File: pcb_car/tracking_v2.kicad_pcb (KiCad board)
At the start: 2 copper layers, 95 x 70 mm, 20 parts, among them J1 Conn_01x02, J2 Conn_01x20_Female, J3 Conn_01x20_Female, J4 Conn_01x02, J5 Conn_01x02, J6 Conn_01x02, J7 Conn_01x02, J8 Conn_01x03, J9 Conn_01x03, SW1 SW_Push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

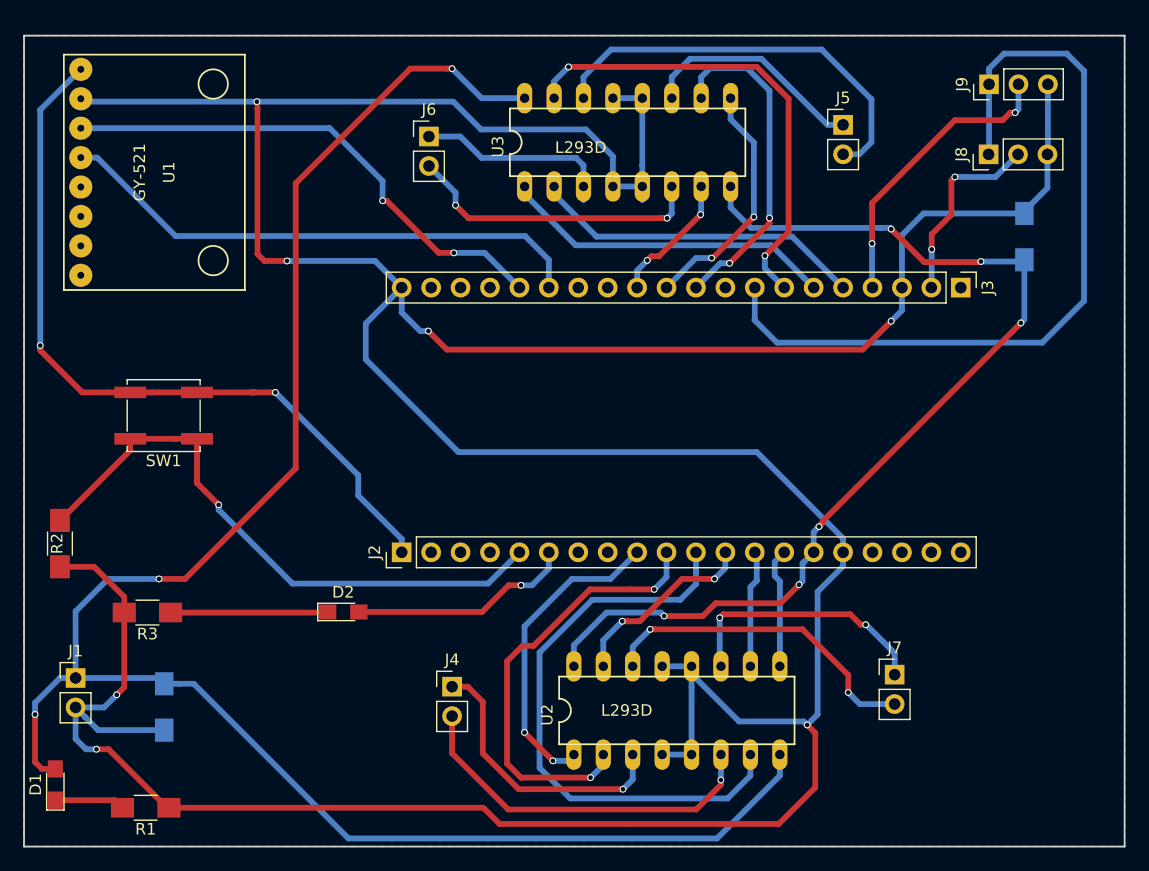
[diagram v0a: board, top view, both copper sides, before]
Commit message: Added second iteration of PCB design (incomplete), moved libraries to subfolder
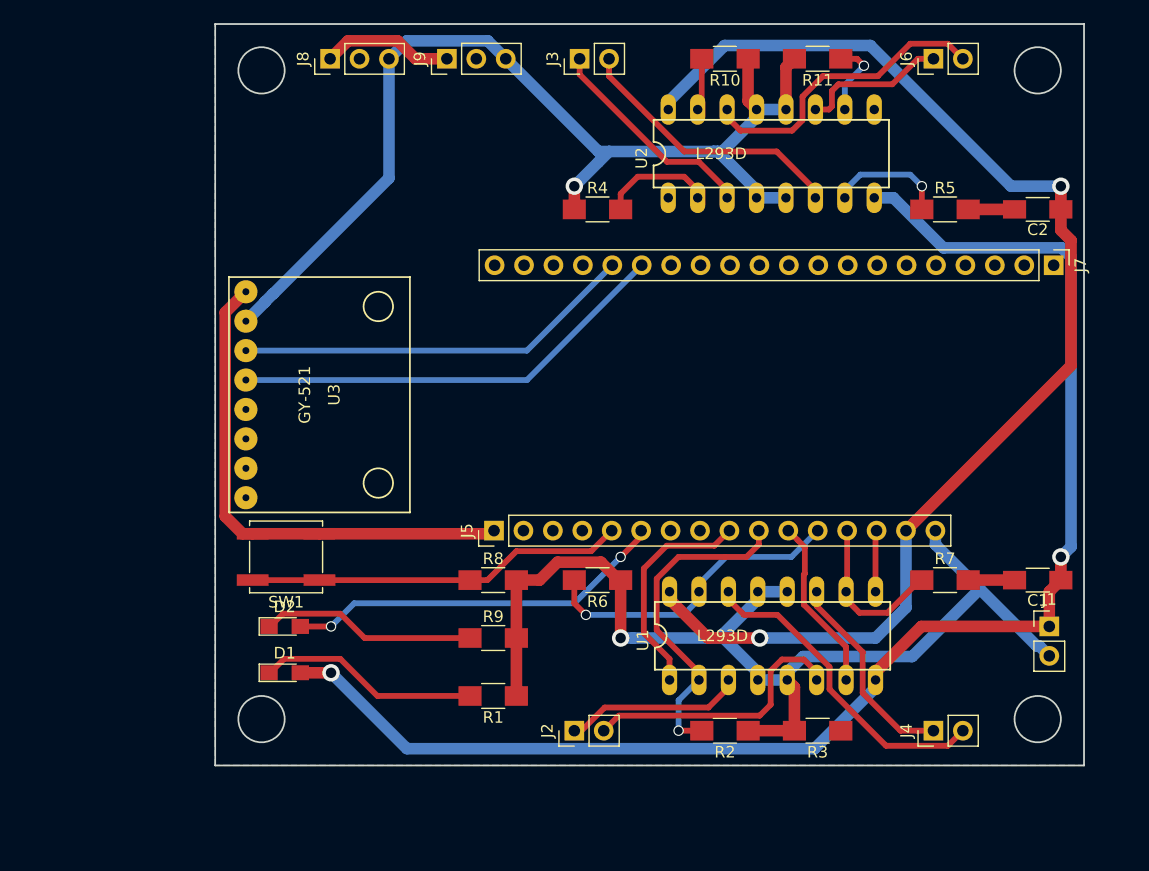
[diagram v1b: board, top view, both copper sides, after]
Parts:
- added R10: R, Resistors_SMD:R_1206_HandSoldering, F.Cu at (163.0, 77.0)
- added R11: R, Resistors_SMD:R_1206_HandSoldering, F.Cu at (171.0, 77.0)
- added R4: R, Resistors_SMD:R_1206_HandSoldering, F.Cu at (152.0, 90.0)
- added R5: R, Resistors_SMD:R_1206_HandSoldering, F.Cu at (182.0, 90.0)
- added R6: R, Resistors_SMD:R_1206_HandSoldering, F.Cu at (152.0, 122.0)
- added R7: R, Resistors_SMD:R_1206_HandSoldering, F.Cu at (182.0, 122.0)
- added R8: R, Resistors_SMD:R_1206_HandSoldering, F.Cu at (143.0, 122.0)
- added R9: R, Resistors_SMD:R_1206_HandSoldering, F.Cu at (143.0, 127.0)
- C1, C2: moved to F.Cu
- J2, J3: value Conn_01x20_Female -> Conn_01x02; footprint Socket_Strips:Socket_Strip_Straight_1x20_Pitch2.54mm -> Pin_Headers:Pin_Header_Straight_1x02_Pitch2.54mm
- J5: value Conn_01x02 -> Conn_01x16_Female; footprint Pin_Headers:Pin_Header_Straight_1x02_Pitch2.54mm -> Socket_Strips:Socket_Strip_Straight_1x16_Pitch2.54mm
- J7: value Conn_01x02 -> Conn_01x20_Female; footprint Pin_Headers:Pin_Header_Straight_1x02_Pitch2.54mm -> Socket_Strips:Socket_Strip_Straight_1x20_Pitch2.54mm
- U1: value GY-521 -> L293D; footprint GY-521:GY-521 -> L293D:DIL16
- U3: value L293D -> GY-521; footprint L293D:DIL16 -> GY-521:GY-521
- moved J1 84.2 mm to (191.0, 126.0)
- moved C1 76.2 mm to (190.0, 122.0), turned to 180 degrees
- moved U1 66.7 mm to (167.1, 126.8), turned to 0 degrees
- moved R2 59.6 mm to (163.0, 135.0), turned to 180 degrees
- moved R3 58.7 mm to (171.0, 135.0)
- moved J8 57.4 mm to (128.9, 77.0)
- moved U2 48.7 mm to (167.0, 85.2)
- moved J9 46.9 mm to (139.0, 77.0)
- moved J5 46.2 mm to (143.1, 117.7), turned to 90 degrees
- moved J6 44.1 mm to (181.0, 77.0), turned to 90 degrees
- moved J4 41.7 mm to (181.0, 135.0), turned to 90 degrees
- moved J3 38.4 mm to (150.5, 77.0), turned to 90 degrees
- moved J7 37.9 mm to (191.4, 94.8), turned to 270 degrees
- moved U3 34.4 mm to (128.0, 106.0), turned to 270 degrees
- moved R1 31.5 mm to (143.0, 132.0)
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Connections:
- J5 pad 1: Net-(J5-Pad1) -> 3v3_gyro
- J7 pad 2: Net-(J7-Pad2) -> DATA2
- J8 pad 2: Net-(J3-Pad2) -> DATA2
- J9 pad 2: Net-(J3-Pad4) -> DATA1
- R2 pad 1: Net-(J2-Pad5) -> GND
- R2 pad 2: GND -> IN1_A
- R3 pad 1: Net-(D2-Pad1) -> IN2_A
- SW1 pad 1: Net-(J2-Pad5) -> Net-(J5-Pad5)
- SW1 pad 2: Net-(J2-Pad1) -> 3v3_gyro
- U1 pad 1: Net-(J2-Pad1) -> EN1_A
- U1 pad 2: GND -> IN1_A
- U1 pad 3: Net-(J3-Pad16) -> Net-(J2-Pad1)
- U1 pad 4: Net-(J3-Pad15) -> GND
- U1 pad 5: Net-(U1-Pad5) -> GND
- U1 pad 6: Net-(U1-Pad6) -> Net-(J2-Pad2)
- U1 pad 7: Net-(U1-Pad7) -> IN2_A
- U1 pad 8: Net-(U1-Pad8) -> BATT
- U2 pad 1: Net-(J2-Pad9) -> EN1_B
- U2 pad 10: Net-(J2-Pad13) -> IN3_B
- U2 pad 11: Net-(J7-Pad1) -> Net-(J6-Pad1)
- U2 pad 14: Net-(J7-Pad2) -> Net-(J6-Pad2)
- U2 pad 15: Net-(J2-Pad12) -> IN4_B
- U2 pad 2: Net-(J2-Pad10) -> IN1_B
- U2 pad 3: Net-(J4-Pad1) -> Net-(J3-Pad1)
- U2 pad 6: Net-(J4-Pad2) -> Net-(J3-Pad2)
- U2 pad 7: Net-(J2-Pad11) -> IN2_B
- U2 pad 9: Net-(J2-Pad14) -> EN2_B
- U3 pad 1: Net-(J3-Pad6) -> 3v3_gyro
- U3 pad 2: Net-(J3-Pad5) -> GND
- U3 pad 3: Net-(J6-Pad1) -> Net-(J7-Pad16)
- U3 pad 4: GND -> Net-(J7-Pad15)
- U3 pad 5: GND -> Net-(U3-Pad5)
- U3 pad 6: Net-(J6-Pad2) -> Net-(U3-Pad6)
- U3 pad 7: Net-(J3-Pad12) -> Net-(U3-Pad7)
- U3 pad 8: 5V -> Net-(U3-Pad8)
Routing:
- net GND: track 371.9 -> 195.7 mm, vias 7 -> 2
- net 3V3: track 70.2 -> 11.4 mm
- net Net-(J2-Pad5): track 52.0 -> 0.00 mm, vias 1 -> 0
- net Net-(J2-Pad1): track 66.2 -> 15.5 mm, vias 2 -> 0
- net Net-(J2-Pad11): track 50.6 -> 0.00 mm
- net Net-(J3-Pad15): track 46.5 -> 0.00 mm
- net Net-(J3-Pad16): track 44.6 -> 0.00 mm, vias 2 -> 0
- net 3v3_gyro: track 0.00 -> 44.1 mm
- net Net-(J3-Pad7): track 41.2 -> 0.00 mm, vias 2 -> 0
- net Net-(J7-Pad15): track 0.00 -> 38.3 mm
- net Net-(J2-Pad10): track 37.9 -> 0.00 mm, vias 2 -> 0
- net BATT: track 161.5 -> 125.4 mm, vias 3 -> 2
- net Net-(J5-Pad2): track 36.0 -> 0.00 mm
- net Net-(J7-Pad16): track 0.00 -> 34.7 mm
- net Net-(J5-Pad5): track 0.00 -> 32.8 mm
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- removed copper zone on F.Cu, net GND
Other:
- board size 95 x 70 mm -> 75 x 64 mm
- net class Default: trace_width 0.25 -> 0.5; via_dia 0.6 -> 0.9; via_drill 0.4 -> 0.7
- net class Power added: clearance 0.2, trace_width 1, via_dia 1.5, via_drill 0.9
- board text added: "Lolin32"

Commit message: Finished second iteration of PCB
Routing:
- net DATA2: track 0.00 -> 71.7 mm
- net DATA1: track 0.00 -> 61.3 mm
- net 3V3: track 11.4 -> 55.1 mm, vias 0 -> 1
- net IN4_B: track 5.19 -> 43.7 mm, vias 0 -> 2
- net EN1_B: track 0.00 -> 23.5 mm, vias 0 -> 1
- net IN1_B: track 9.75 -> 32.7 mm, vias 0 -> 1
- net EN2_B: track 0.66 -> 23.5 mm, vias 0 -> 2
- net IN3_B: track 7.37 -> 28.5 mm
- net IN2_B: track 10.3 -> 23.0 mm
- net GND: track 195.7 -> 204.5 mm
- net BATT: track 125.4 -> 124.8 mm

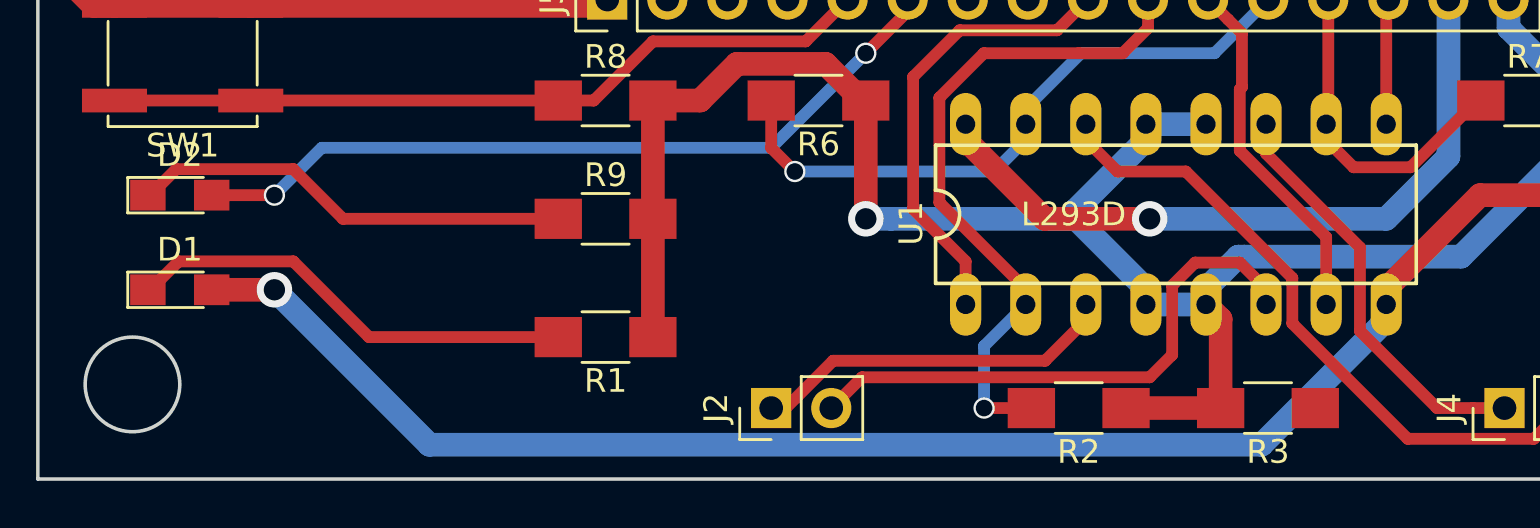
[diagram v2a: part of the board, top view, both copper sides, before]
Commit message: Minor improvements to PCB
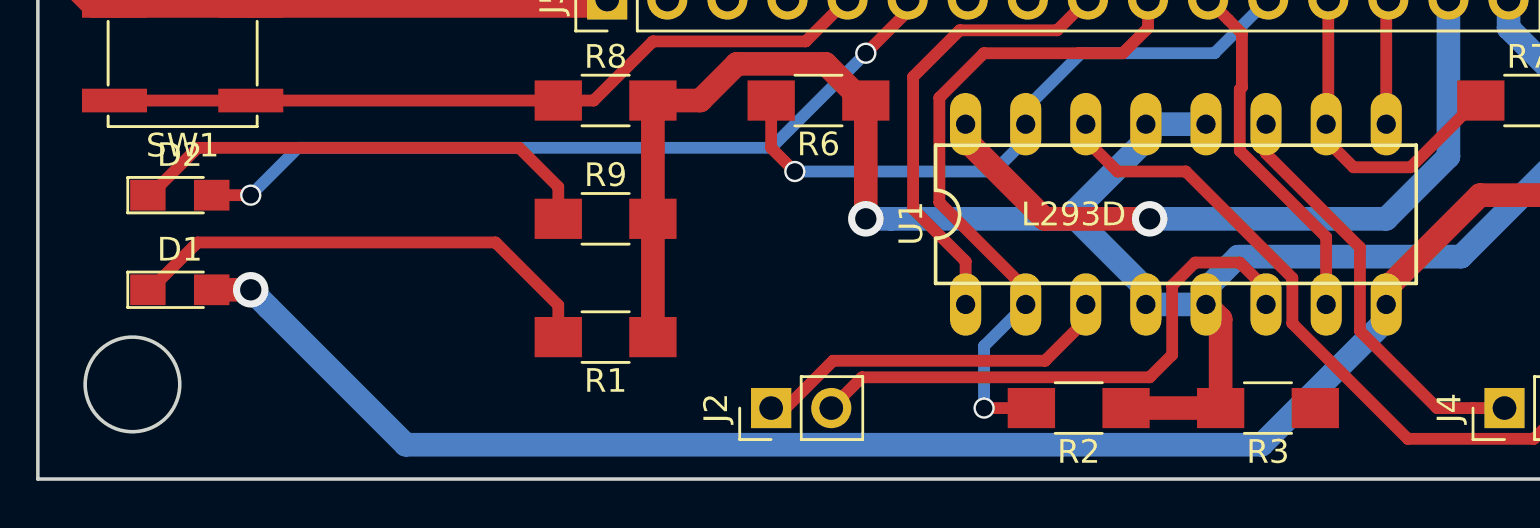
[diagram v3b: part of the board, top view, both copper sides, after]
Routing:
- net Net-(D2-Pad1): track 18.7 -> 20.2 mm
- net Net-(D1-Pad1): track 19.2 -> 20.6 mm
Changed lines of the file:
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@@
     (thickness 1.6)
     (drawings 36)
-    (tracks 340)
+    (tracks 342)
     (zones 0)
     (modules 28)
@@
   (gr_line (start 194 119) (end 138 119) (layer Dwgs.User) (width 0.2))
   (gr_line (start 194 94.5) (end 194 119) (layer Dwgs.User) (width 0.2))
-  (segment (start 141 132) (end 133 132) (width 0.5) (layer F.Cu) (net 1))
-  (segment (start 133 132) (end 129.799999 128.799999) (width 0.5) (layer F.Cu) (net 1))
-  (segment (start 129.799999 128.799999) (end 124.950001 128.799999) (width 0.5) (layer F.Cu) (net 1))
-  (segment (start 124.950001 128.799999) (end 123.75 130) (width 0.5) (layer F.Cu) (net 1))
-  (segment (start 123.75 130) (end 123.65 130) (width 0.5) (layer F.Cu) (net 1))
+  (segment (start 141 130.65) (end 138.35 128) (width 0.5) (layer F.Cu) (net 1))
+  (segment (start 123.65 130) (end 123.75 130) (width 0.5) (layer F.Cu) (net 1))
+  (segment (start 125.75 128) (end 138.35 128) (width 0.5) (layer F.Cu) (net 1))
+  (segment (start 123.75 130) (end 125.75 128) (width 0.5) (layer F.Cu) (net 1))
+  (segment (start 141 132) (end 141 130.65) (width 0.5) (layer F.Cu) (net 1))
+  (segment (start 128.749999 130.749999) (end 128 130) (width 1) (layer B.Cu) (net 2))
+  (segment (start 134.550001 136.550001) (end 128.749999 130.749999) (width 1) (layer B.Cu) (net 2))
+  (segment (start 170.730399 136.550001) (end 134.550001 136.550001) (width 1) (layer B.Cu) (net 2))
+  (segment (start 176 131.2804) (end 170.730399 136.550001) (width 1) (layer B.Cu) (net 2))
+  (segment (start 176 130.62) (end 176 131.2804) (width 1) (layer B.Cu) (net 2))
+  (segment (start 126.35 130) (end 128 130) (width 1) (layer F.Cu) (net 2))
+  (via (at 128 130) (size 1.5) (drill 0.9) (layers F.Cu B.Cu) (net 2))
   (segment (start 192 120) (end 192 122) (width 1) (layer F.Cu) (net 2))
   (segment (start 193 93.479998) (end 193 119) (width 1) (layer B.Cu) (net 2))
@@
   (segment (start 181.013515 93.269999) (end 192.790001 93.269999) (width 1) (layer B.Cu) (net 2))
   (segment (start 192.790001 93.269999) (end 193 93.479998) (width 1) (layer B.Cu) (net 2))
-  (segment (start 129 130) (end 135.550001 136.550001) (width 1) (layer B.Cu) (net 2))
-  (segment (start 135.550001 136.550001) (end 170.730399 136.550001) (width 1) (layer B.Cu) (net 2))
-  (segment (start 170.730399 136.550001) (end 176 131.2804) (width 1) (layer B.Cu) (net 2))
-  (segment (start 176 131.2804) (end 176 130.62) (width 1) (layer B.Cu) (net 2))
-  (segment (start 126.35 130) (end 129 130) (width 1) (layer F.Cu) (net 2))
-  (via (at 129 130) (size 1.5) (drill 0.9) (layers F.Cu B.Cu) (net 2))
   (segment (start 191 126) (end 191 123) (width 1) (layer F.Cu) (net 2))
   (segment (start 191 123) (end 192 122) (width 1) (layer F.Cu) (net 2))
@@
   (segment (start 176 129.9596) (end 176 130.62) (width 1) (layer F.Cu) (net 2))
   (segment (start 179.9596 126) (end 176 129.9596) (width 1) (layer F.Cu) (net 2))
-  (segment (start 141 127) (end 131.899999 127) (width 0.5) (layer F.Cu) (net 3))
-  (segment (start 124.850001 124.899999) (end 123.75 126) (width 0.5) (layer F.Cu) (net 3))
-  (segment (start 131.899999 127) (end 129.799998 124.899999) (width 0.5) (layer F.Cu) (net 3))
-  (segment (start 129.799998 124.899999) (end 124.850001 124.899999) (width 0.5) (layer F.Cu) (net 3))
+  (segment (start 139.35 124) (end 125.75 124) (width 0.5) (layer F.Cu) (net 3))
+  (segment (start 125.75 124) (end 123.75 126) (width 0.5) (layer F.Cu) (net 3))
   (segment (start 123.75 126) (end 123.65 126) (width 0.5) (layer F.Cu) (net 3))
+  (segment (start 141 127) (end 141 125.65) (width 0.5) (layer F.Cu) (net 3))
+  (segment (start 141 125.65) (end 139.35 124) (width 0.5) (layer F.Cu) (net 3))
+  (segment (start 126.35 126) (end 128 126) (width 0.5) (layer F.Cu) (net 4))
+  (segment (start 131 124) (end 130 124) (width 0.5) (layer B.Cu) (net 4))
+  (segment (start 130 124) (end 128 126) (width 0.5) (layer B.Cu) (net 4))
+  (via (at 128 126) (size 0.9) (drill 0.7) (layers F.Cu B.Cu) (net 4))
   (segment (start 150 124) (end 131 124) (width 0.5) (layer B.Cu) (net 4))
-  (segment (start 131 124) (end 129 126) (width 0.5) (layer B.Cu) (net 4))
   (segment (start 154 120) (end 150 124) (width 0.5) (layer B.Cu) (net 4))
   (segment (start 155.77 117.73) (end 155.77 118.23) (width 0.5) (layer F.Cu) (net 4))
@@
   (via (at 154 120) (size 0.9) (drill 0.7) (layers F.Cu B.Cu) (net 4))
   (segment (start 156 117.96) (end 155.77 117.73) (width 0.5) (layer F.Cu) (net 4))
-  (segment (start 126.35 126) (end 129 126) (width 0.5) (layer F.Cu) (net 4))
-  (via (at 129 126) (size 0.9) (drill 0.7) (layers F.Cu B.Cu) (net 4))
   (segment (start 150 90) (end 147.94 90) (width 1) (layer F.Cu) (net 5))
   (segment (start 147.94 90) (end 143.12 94.82) (width 1) (layer F.Cu) (net 5))

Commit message: updated
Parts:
- removed R11, R3, R5, R7: R, Resistors_SMD:R_1206_HandSoldering
- moved R6 29.7 mm to (181.7, 123.0)
- moved R10 23.5 mm to (183.3, 88.7), turned to 90 degrees
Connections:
- R10 pad 2: IN4_B -> EN2_B
- R2 pad 2: IN1_A -> EN1_A
- R4 pad 2: IN1_B -> EN1_B
- R6 pad 2: IN4_A -> EN2_A
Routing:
- net IN4_A: track 27.9 -> 13.5 mm, vias 1 -> 0
- net EN2_B: track 23.5 -> 34.0 mm
- net IN1_B: track 32.7 -> 23.0 mm
- net IN2_B: track 23.0 -> 13.4 mm, vias 1 -> 0
- net IN3_A: track 14.2 -> 5.31 mm
- net IN1_A: track 28.6 -> 21.5 mm, vias 1 -> 0
- net IN3_B: track 28.5 -> 21.5 mm, vias 1 -> 0
- net EN1_A: track 19.9 -> 26.6 mm, vias 0 -> 1
- net EN1_B: track 23.5 -> 28.7 mm
- net IN4_B: track 43.7 -> 39.2 mm
- net EN2_A: track 5.31 -> 8.98 mm
- net GND: track 204.5 -> 207.0 mm, vias 2 -> 3
